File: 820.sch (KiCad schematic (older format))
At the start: 126 parts, among them J1 PJ301BM, J10 PJ301BM, J2 PJ301BM, J3 PJ301BM, J4 PJ301BM, J5 PJ301BM, J6 PJ301BM, J7 PJ301BM, J8 PJ301BM, J9 PJ301BM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

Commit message: starting to place and route
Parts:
- removed J3: PJ301BM, MyModules:PJ-301B-JACK-SLOTS, symbol JACK_MONO_SW
- removed R14: 100K, MyModules:SM0603-R-JRL, symbol R_US
- removed VR4: 100K(A), MyModules:RD901F-ALPHA-POT-T18, symbol POT_US
- U1: footprint MyModules:TSSOP8-JRL -> Housings_SSOP:MSOP-8_3x3mm_Pitch0.65mm
- VR3: value 100K(A) -> 100K(B)
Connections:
- net GND: now also Q1.1 (B); no longer Q1.3 (B)
- net at R17.2, TC1.1: now also Q1.3 (B); no longer Q1.1 (B)
- net at C15.1, R18.1, U1.6 (-): now also Q1.4 (C); no longer Q1.5 (C)
- net at R21.1, U2.2 (-): now also Q1.5 (C); no longer Q1.4 (C)
- no-connect marks 12 -> 11
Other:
- moved on the sheet: Q1A, Q1B

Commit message: mostly placed
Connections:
- net +10V: now also VR9.3; no longer VR9.1
- net +12V: now also VR10.3; no longer VR10.1
- net -10V: now also VR9.1; no longer VR9.3
- net at R35.2: now also VR10.1; no longer VR10.3
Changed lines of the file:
@@
 F 3 "" H 13050 11300 60  0000 C CNN
 	1    13050 11300
-	0    1    1    0
+	0    1    -1   0
 $EndComp
 $Comp
@@
 F 3 "" H 15675 9300 60  0000 C CNN
 	1    15675 9300
-	0    -1   1    0
-$EndComp
-$Comp
+	0    -1   -1   0
+$EndComp
+$Comp

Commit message: separated rotary switch daughter board, finished routing
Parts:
- added C21: 0.1µ, MyModules:SM0603-C-JRL, symbol C_US
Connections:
- net +12V: now also C21.1
- net GND: now also C21.2
- net at P4.2 (P2): now also SW2.7; no longer SW2.1
- net at P4.5 (P5): now also SW2.4; no longer SW2.10
- net at P4.4 (P4): now also SW2.5; no longer SW2.11
- net at P4.3 (P3): now also SW2.6; no longer SW2.12
- net at P4.1 (P1): now also SW2.8; no longer SW2.2 (8)
- net at P4.6 (P6), P4.7 (P7): now also SW2.3; no longer SW2.9
- net at P4.8 (P8): now also SW2.D; no longer SW2.A
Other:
- note added: "INVERTING OUTPUT?"

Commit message: bit of tweaking, need to start placing references
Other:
- note added: "FEEDBACK CAP?"
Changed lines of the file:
@@
 	3025 2500 3025 2000
 Connection ~ 2875 2500
+Text Notes 15850 13275 0    60   ~ 0
+FEEDBACK CAP?
 $EndSCHEMATC

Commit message: fixed incorrect pin on switch board: 9 was connected instead of 8
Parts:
- R18: value 1.5M -> 1meg
- R43: value 8.2K -> 7.5K
- R47: value 10K -> 12K
- R48: value 15K -> 10K
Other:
- note added: "1meg for \nIref = 10µA"
- note added: "7.5K for symmetry \naround 0V - needed \nfor symmetrical sine"
- note added: "INVERTING OUTPUT?\nWould allow a little gain\nto be applied here"
- note added: "R91 CHANGED TO 12K"
- note removed: "1M?"
- note removed: "9.1K? - need a bit more +ve offset\nto prevent clipping in CD4052 (-5V MAX)"
- note removed: "INVERTING OUTPUT?"
- note removed: "R91 CHANGED BACK\nTO 10K - TOO MUCH GAIN\nCAUSED CLIPPING"
- note removed: "R91 CHANGED TO 15K"
- note removed: "R95 CHANGED TO 15K"
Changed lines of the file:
@@
 P 12225 6775
 F 0 "R18" H 12100 6725 50  0000 C CNN
-F 1 "1.5M" H 12100 6800 50  0000 C CNN
+F 1 "1meg" H 12100 6800 50  0000 C CNN
 F 2 "MyModules:SM0603-R-JRL" H 12225 6775 60  0001 C CNN
 F 3 "" H 12225 6775 60  0001 C CNN
@@
 P 18125 7075
 F 0 "R47" V 18200 7250 50  0000 C CNN
-F 1 "10K" V 18175 6900 50  0000 C CNN
+F 1 "12K" V 18175 6900 50  0000 C CNN
 F 2 "MyModules:SM0603-R-JRL" H 18125 7075 60  0001 C CNN
 F 3 "" H 18125 7075 60  0001 C CNN
@@
 $EndComp
 $Comp
-L R_US R43
-U 1 1 5B4130BE
-P 17575 6550
-F 0 "R43" H 17450 6575 50  0000 C CNN
-F 1 "8.2K" H 17425 6650 50  0000 C CNN
-F 2 "MyModules:SM0603-R-JRL" H 17575 6550 60  0001 C CNN
-F 3 "" H 17575 6550 60  0001 C CNN
-F 4 "P10.0KCCT-ND" V 17575 6550 60  0001 C CNN "Digikey"
-	1    17575 6550
-	-1   0    0    1
-$EndComp
-$Comp
 L +12V #PWR69
 U 1 1 5B4130C5
@@
 P 18650 9700
 F 0 "R48" V 18725 9875 50  0000 C CNN
-F 1 "15K" V 18700 9525 50  0000 C CNN
+F 1 "10K" V 18700 9525 50  0000 C CNN
 F 2 "MyModules:SM0603-R-JRL" H 18650 9700 60  0001 C CNN
 F 3 "" H 18650 9700 60  0001 C CNN
@@
 	0    -1   -1   0
 $EndComp
-Text Notes 18150 9850 0    60   ~ 0
-R95 CHANGED TO 15K
 $Comp
 L R_US R38
@@
 Text Notes 7150 9000 0    60   ~ 0
 0.1%
-Text Notes 12450 6825 0    60   ~ 0
-1M?
+Text Notes 12150 6850 2    60   ~ 0
+1meg for \nIref = 10µA
 Text Notes 17675 7225 0    60   ~ 0
-R91 CHANGED TO 15K
-Text Notes 18750 7400 0    60   ~ 0
-R91 CHANGED BACK\nTO 10K - TOO MUCH GAIN\nCAUSED CLIPPING
-Text Notes 17625 6475 0    60   ~ 0
-9.1K? - need a bit more +ve offset\nto prevent clipping in CD4052 (-5V MAX)
+R91 CHANGED TO 12K
+Text Notes 17700 6500 0    60   ~ 0
+7.5K for symmetry \naround 0V - needed \nfor symmetrical sine
 Text Notes 9775 8550 0    60   ~ 0
 OPA2180 low drift?\nTried, works.\nNeeds new footprint
@@
 Text Notes 17525 15700 0    200  ~ 40
 820\n
-Text Notes 18425 11950 0    60   ~ 0
-INVERTING OUTPUT?
+Text Notes 18350 12075 0    60   ~ 0
+INVERTING OUTPUT?\nWould allow a little gain\nto be applied here
 $Comp
 L C_US C21
@@
 Text Notes 15850 13275 0    60   ~ 0
 FEEDBACK CAP?
+$Comp
+L R_US R43
+U 1 1 5B4130BE
+P 17575 6550
+F 0 "R43" H 17450 6575 50  0000 C CNN
+F 1 "7.5K" H 17425 6650 50  0000 C CNN
+F 2 "MyModules:SM0603-R-JRL" H 17575 6550 60  0001 C CNN
+F 3 "" H 17575 6550 60  0001 C CNN
+F 4 "P10.0KCCT-ND" V 17575 6550 60  0001 C CNN "Digikey"
+	1    17575 6550
+	-1   0    0    1
+$EndComp
 $EndSCHEMATC

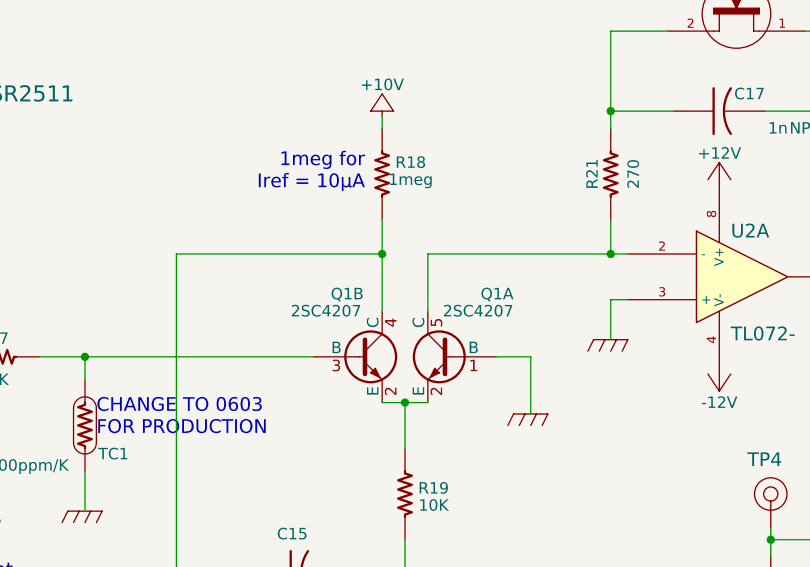
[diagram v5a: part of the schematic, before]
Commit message: changed 2SC4207 NPN pair to BCM847 matched pair.
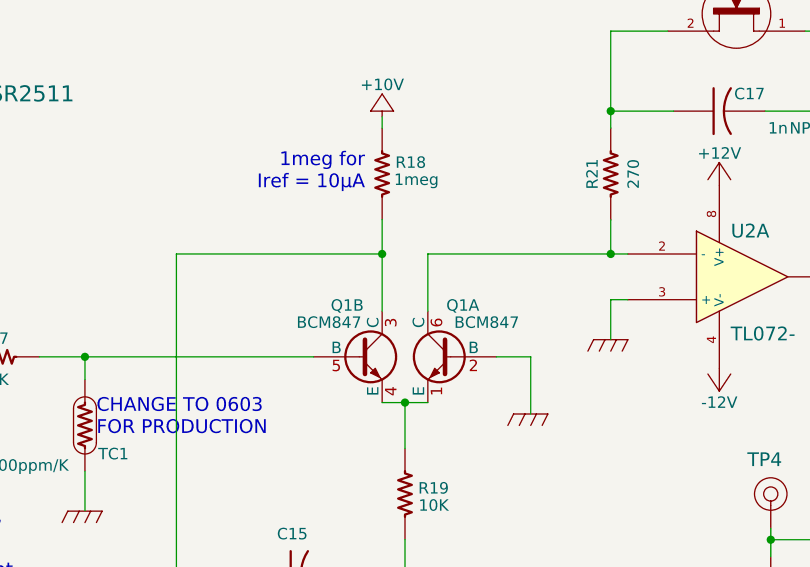
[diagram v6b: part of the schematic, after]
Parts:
- removed Q1: 2SC4207, MyModules:SOT753_TSOP5_SC-74A, symbol 2SC4207
- added Q1: BCM847, TO_SOT_Packages_SMD:SOT-666, symbol BCM847
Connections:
- net GND: now also Q1.2 (B)
- net at R17.2, TC1.1: now also Q1.5 (B)
- net at C15.1, R18.1, U1.6 (-): now also Q1.3 (C)
- net at R19.2: now also Q1.1 (E), Q1.4 (E)
- net at R21.1, U2.2 (-): now also Q1.6 (C)

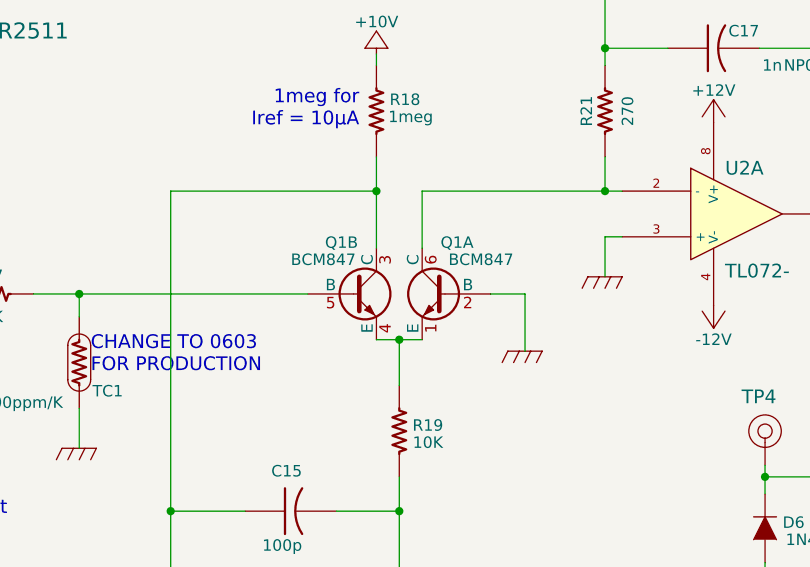
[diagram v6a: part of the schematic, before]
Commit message: PMP4201 NPN matched pair replaces BCM847
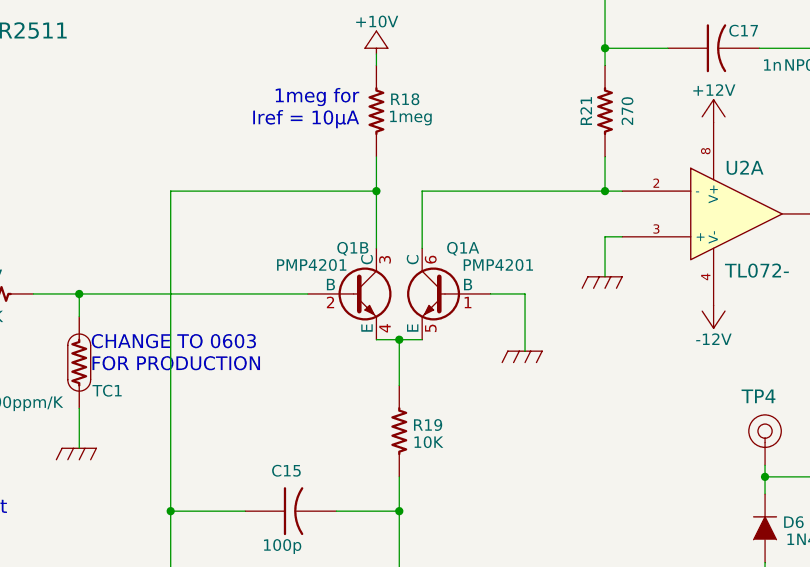
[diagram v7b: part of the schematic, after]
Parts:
- removed Q1: BCM847, TO_SOT_Packages_SMD:SOT-666, symbol BCM847
- added Q1: PMP4201, TO_SOT_Packages_SMD:SOT-666, symbol PMP4201
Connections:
- net GND: now also Q1.1 (B)
- net at R17.2, TC1.1: now also Q1.2 (B)
- net at C15.1, R18.1, U1.6 (-): now also Q1.3 (C)
- net at R19.2: now also Q1.4 (E), Q1.5 (E)
- net at R21.1, U2.2 (-): now also Q1.6 (C)
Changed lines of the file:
@@
 $EndComp
 $Comp
-L BCM847 Q1
-U 1 1 5BCE4EF8
+L PMP4201 Q1
+U 1 1 5BD09BB5
 P 12525 7575
-F 0 "Q1" H 12400 7800 50  0000 L CNN
-F 1 "BCM847" H 12225 7725 50  0000 L CNN
+F 0 "Q1" H 12375 7775 50  0000 L CNN
+F 1 "PMP4201" H 12950 7700 50  0000 L CNN
 F 2 "TO_SOT_Packages_SMD:SOT-666" H 12725 7500 50  0001 L CIN
 F 3 "" H 12525 7575 50  0000 L CNN
@@
 $EndComp
 $Comp
-L BCM847 Q1
-U 2 1 5BCE5095
+L PMP4201 Q1
+U 2 1 5BD0A26C
 P 12125 7575
-F 0 "Q1" H 12000 7800 50  0000 L CNN
-F 1 "BCM847" H 11850 7725 50  0000 L CNN
+F 0 "Q1" H 12050 7775 50  0000 L CNN
+F 1 "PMP4201" H 12600 7700 50  0000 L CNN
 F 2 "TO_SOT_Packages_SMD:SOT-666" H 12325 7500 50  0001 L CIN
 F 3 "" H 12125 7575 50  0000 L CNN

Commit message: first commit in a while. switched matched pair to PMP and other stuff. getting ready to order r1.1
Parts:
- added R14: 16.9R, MyModules:SM0603-R-JRL, symbol R_US
- TC1: value 1K 3300ppm/K -> 500R ±3850ppm/°C
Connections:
- net GND: now also R14.1; no longer TC1.2
- new net: R14.2, TC1.2
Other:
- note removed: "CHANGE TO 0603\nFOR PRODUCTION"
- note removed: "OPA2180 low drift?\nTried, works.\nNeeds new footprint"
